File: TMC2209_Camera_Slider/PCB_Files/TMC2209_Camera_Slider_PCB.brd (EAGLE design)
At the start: 100 x 70 mm, 21 parts, among them J1 1X2-3.5MM

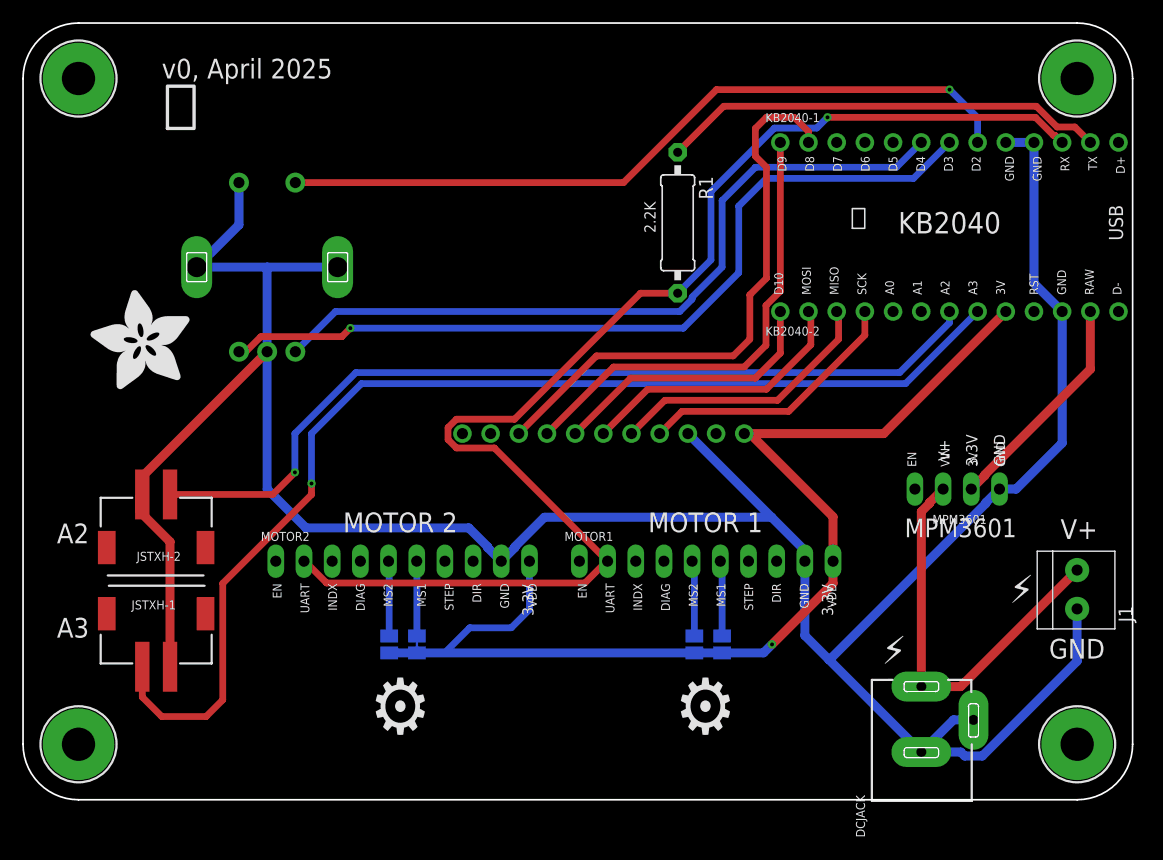
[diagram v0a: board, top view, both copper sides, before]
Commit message: switch jst xh connectors
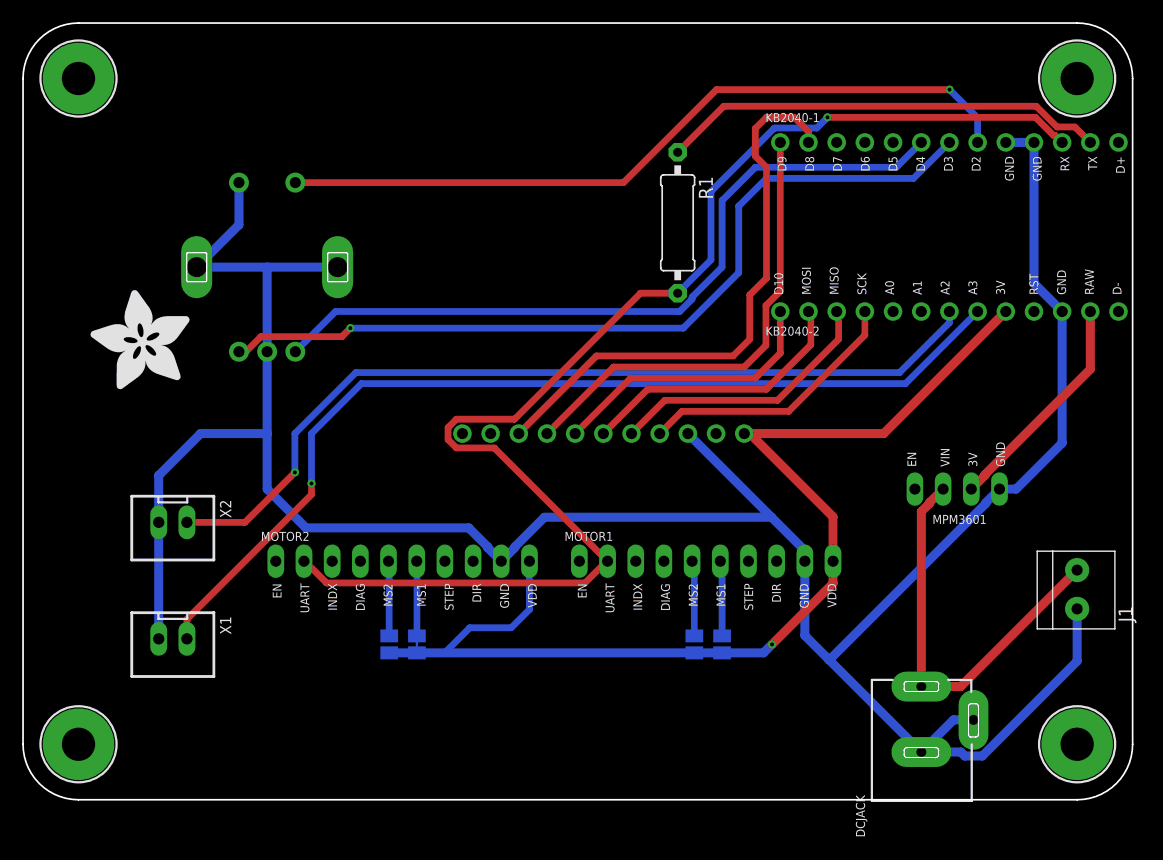
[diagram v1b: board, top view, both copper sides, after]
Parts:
- removed JSTXH-1, JSTXH-2: CON_JST_XH_2PIN-VERT, adafruit_electromech:JST-XH-2-SV
- added PLABEL0: (no value), pinguin:PLABEL0
- added PLABEL1: (no value), pinguin:PLABEL1
- added PLABEL10: (no value), pinguin:PLABEL10
- added PLABEL11: (no value), pinguin:PLABEL11
- added PLABEL12: (no value), pinguin:PLABEL12
- added PLABEL13: (no value), pinguin:PLABEL13
- added PLABEL14: (no value), pinguin:PLABEL14
- added PLABEL15: (no value), pinguin:PLABEL15
- added PLABEL16: (no value), pinguin:PLABEL16
- added PLABEL17: (no value), pinguin:PLABEL17
- added PLABEL18: (no value), pinguin:PLABEL18
- added PLABEL19: (no value), pinguin:PLABEL19
- added PLABEL2: (no value), pinguin:PLABEL2
- added PLABEL20: (no value), pinguin:PLABEL20
- added PLABEL21: (no value), pinguin:PLABEL21
- added PLABEL22: (no value), pinguin:PLABEL22
- added PLABEL23: (no value), pinguin:PLABEL23
- added PLABEL24: (no value), pinguin:PLABEL24
- added PLABEL25: (no value), pinguin:PLABEL25
- added PLABEL26: (no value), pinguin:PLABEL26
- added PLABEL27: (no value), pinguin:PLABEL27
- added PLABEL28: (no value), pinguin:PLABEL28
- added PLABEL29: (no value), pinguin:PLABEL29
- added PLABEL3: (no value), pinguin:PLABEL3
- added PLABEL30: (no value), pinguin:PLABEL30
- added PLABEL31: (no value), pinguin:PLABEL31
- added PLABEL32: (no value), pinguin:PLABEL32
- added PLABEL33: (no value), pinguin:PLABEL33
- added PLABEL34: (no value), pinguin:PLABEL34
- added PLABEL35: (no value), pinguin:PLABEL35
- added PLABEL36: (no value), pinguin:PLABEL36
- added PLABEL37: (no value), pinguin:PLABEL37
- added PLABEL38: (no value), pinguin:PLABEL38
- added PLABEL39: (no value), pinguin:PLABEL39
- added PLABEL4: (no value), pinguin:PLABEL4
- added PLABEL40: (no value), pinguin:PLABEL40
- added PLABEL41: (no value), pinguin:PLABEL41
- added PLABEL42: (no value), pinguin:PLABEL42
- added PLABEL43: (no value), pinguin:PLABEL43
- added PLABEL44: (no value), pinguin:PLABEL44
- added PLABEL45: (no value), pinguin:PLABEL45
- added PLABEL46: (no value), pinguin:PLABEL46
- added PLABEL47: (no value), pinguin:PLABEL47
- added PLABEL48: (no value), pinguin:PLABEL48
- added PLABEL49: (no value), pinguin:PLABEL49
- added PLABEL5: (no value), pinguin:PLABEL5
- added PLABEL50: (no value), pinguin:PLABEL50
- added PLABEL51: (no value), pinguin:PLABEL51
- added PLABEL52: (no value), pinguin:PLABEL52
- added PLABEL53: (no value), pinguin:PLABEL53
- added PLABEL54: (no value), pinguin:PLABEL54
- added PLABEL55: (no value), pinguin:PLABEL55
- added PLABEL56: (no value), pinguin:PLABEL56
- added PLABEL57: (no value), pinguin:PLABEL57
- added PLABEL58: (no value), pinguin:PLABEL58
- added PLABEL59: (no value), pinguin:PLABEL59
- added PLABEL6: (no value), pinguin:PLABEL6
- added PLABEL60: (no value), pinguin:PLABEL60
- added PLABEL61: (no value), pinguin:PLABEL61
- added PLABEL62: (no value), pinguin:PLABEL62
- added PLABEL63: (no value), pinguin:PLABEL63
- added PLABEL64: (no value), pinguin:PLABEL64
- added PLABEL65: (no value), pinguin:PLABEL65
- added PLABEL66: (no value), pinguin:PLABEL66
- added PLABEL67: (no value), pinguin:PLABEL67
- added PLABEL68: (no value), pinguin:PLABEL68
- added PLABEL69: (no value), pinguin:PLABEL69
- added PLABEL70: (no value), pinguin:PLABEL70
- added PLABEL71: (no value), pinguin:PLABEL71
- added PLABEL72: (no value), pinguin:PLABEL72
- added PLABEL73: (no value), pinguin:PLABEL73
- added PLABEL74: (no value), pinguin:PLABEL74
- added PLABEL75: (no value), pinguin:PLABEL75
- added PLABEL76: (no value), pinguin:PLABEL76
- added PLABEL77: (no value), pinguin:PLABEL77
- added PLABEL78: (no value), pinguin:PLABEL78
- added PLABEL79: (no value), pinguin:PLABEL79
- added PLABEL8: (no value), pinguin:PLABEL8
- added PLABEL80: (no value), pinguin:PLABEL80
- added PLABEL81: (no value), pinguin:PLABEL81
- added PLABEL82: (no value), pinguin:PLABEL82
- added PLABEL83: (no value), pinguin:PLABEL83
- added PLABEL84: (no value), pinguin:PLABEL84
- added PLABEL85: (no value), pinguin:PLABEL85
- added PLABEL86: (no value), pinguin:PLABEL86
- added PLABEL87: (no value), pinguin:PLABEL87
- added PLABEL88: (no value), pinguin:PLABEL88
- added PLABEL89: (no value), pinguin:PLABEL89
- added PLABEL9: (no value), pinguin:PLABEL9
- added PLABEL90: (no value), pinguin:PLABEL90
- added PLABEL91: (no value), pinguin:PLABEL91
- added PLABEL92: (no value), pinguin:PLABEL92
- added PLABEL93: (no value), pinguin:PLABEL93
- added X1, X2: REMBRANDT-ELECTRONICS---JST-XH-CONNECTORS-V1-0_JST-XH-02-PI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, thermalBonnet:REMBRANDT-ELECTRONICS---JST-XH-CONNECTORS-V1-0_JST-XH-02-PACKAGE-LONG-PAD
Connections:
- net A2: now also X2.1; no longer JSTXH-2.1
- net A3: now also X1.1; no longer JSTXH-1.1
- net GND: now also X1.2, X2.2; no longer JSTXH-1.2, JSTXH-2.2
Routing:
- net A3: track 103.2 -> 87.7 mm
- net GND: track 251.7 -> 243.4 mm

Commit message: miso/mosi
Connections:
- removed net MI: KB2040-2.3, TFT.7
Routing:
- net MI: track 24.8 -> 0.00 mm
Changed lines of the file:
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@@
 <wire x1="75.87" y1="41.87" x2="75.87" y2="44" width="0.6096" layer="1"/>
-</signal>
-<signal name="MI">
-<contactref element="KB2040-2" pad="3"/>
-<contactref element="TFT" pad="7"/>
-<wire x1="54.84" y1="33" x2="57.84" y2="36" width="0.6096" layer="1"/>
-<wire x1="68" y1="36" x2="73.5" y2="41.5" width="0.6096" layer="1"/>
-<wire x1="73.5" y1="41.5" x2="73.5" y2="43.83" width="0.6096" layer="1"/>
-<wire x1="73.5" y1="43.83" x2="73.33" y2="44" width="0.6096" layer="1"/>
-<wire x1="57.84" y1="36" x2="68" y2="36" width="0.6096" layer="1"/>
 </signal>
 <signal name="MS1_2">
@@
 </signal>
 <signal name="MO">
-<contactref element="KB2040-2" pad="2"/>
 <contactref element="TFT" pad="6"/>
 <wire x1="52.3" y1="33" x2="56.3" y2="37" width="0.6096" layer="1"/>
-<wire x1="71" y1="43.79" x2="70.79" y2="44" width="0.6096" layer="1"/>
 <wire x1="56.3" y1="37" x2="67" y2="37" width="0.6096" layer="1"/>
 <wire x1="67" y1="37" x2="71" y2="41" width="0.6096" layer="1"/>
+<contactref element="KB2040-2" pad="2"/>
 <wire x1="71" y1="41" x2="71" y2="43.79" width="0.6096" layer="1"/>
+<wire x1="71" y1="43.79" x2="70.79" y2="44" width="0.6096" layer="1"/>
 </signal>
 <signal name="CS">
